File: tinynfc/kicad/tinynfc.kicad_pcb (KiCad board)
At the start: 2 copper layers, 28 x 28 mm, 15 parts, among them Q1 Diodes_DFN1006-3, U1 NXP_SOT902-3_XQFN8, U2 VQFN-20-1EP_3x3mm_P0.4mm_EP1.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

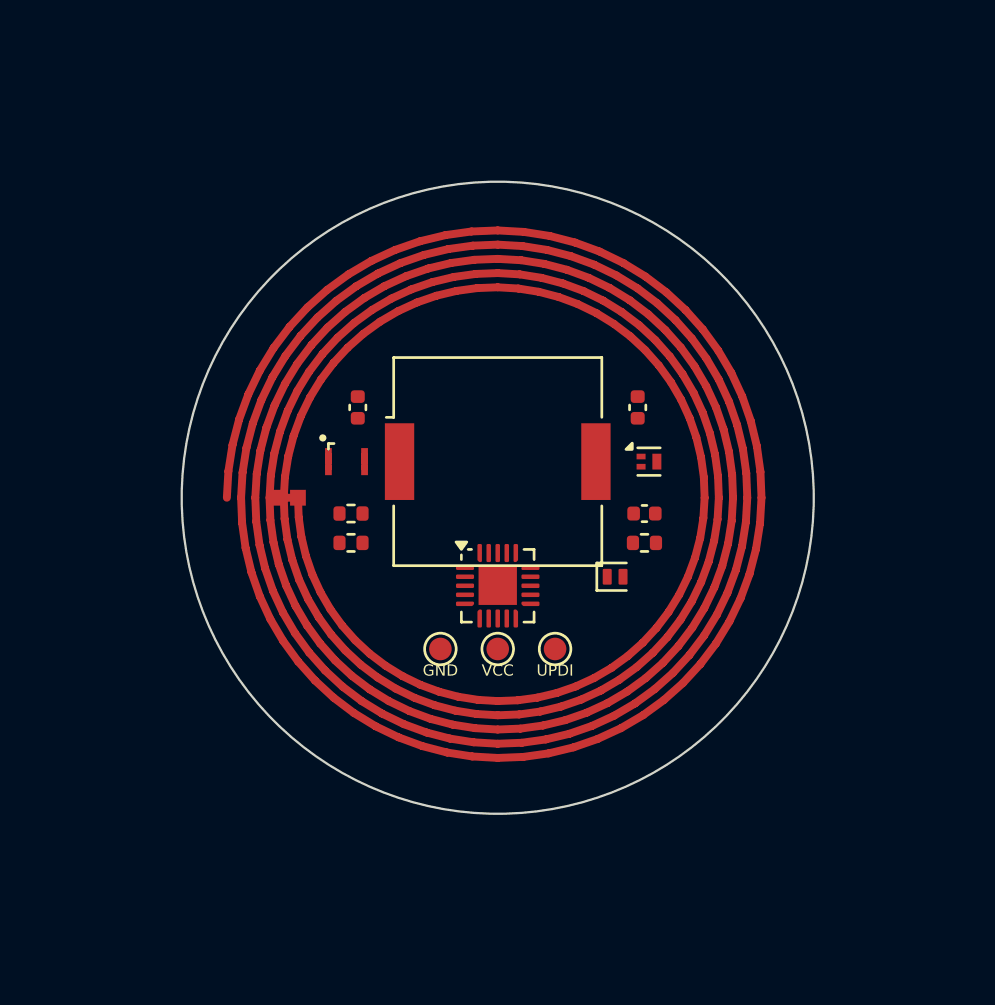
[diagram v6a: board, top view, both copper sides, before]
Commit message: Shrink TinyNFC board to exact US-quarter diameter
Trim the FR-4 ring outside the spiral: outline is Ø 24.26 mm, antenna
Ø 23 mm with ~0.5 mm copper-to-edge, parts pulled into the tighter island.

Co-authored-by: Jason Hall <imjasonh@users.noreply.github.com>
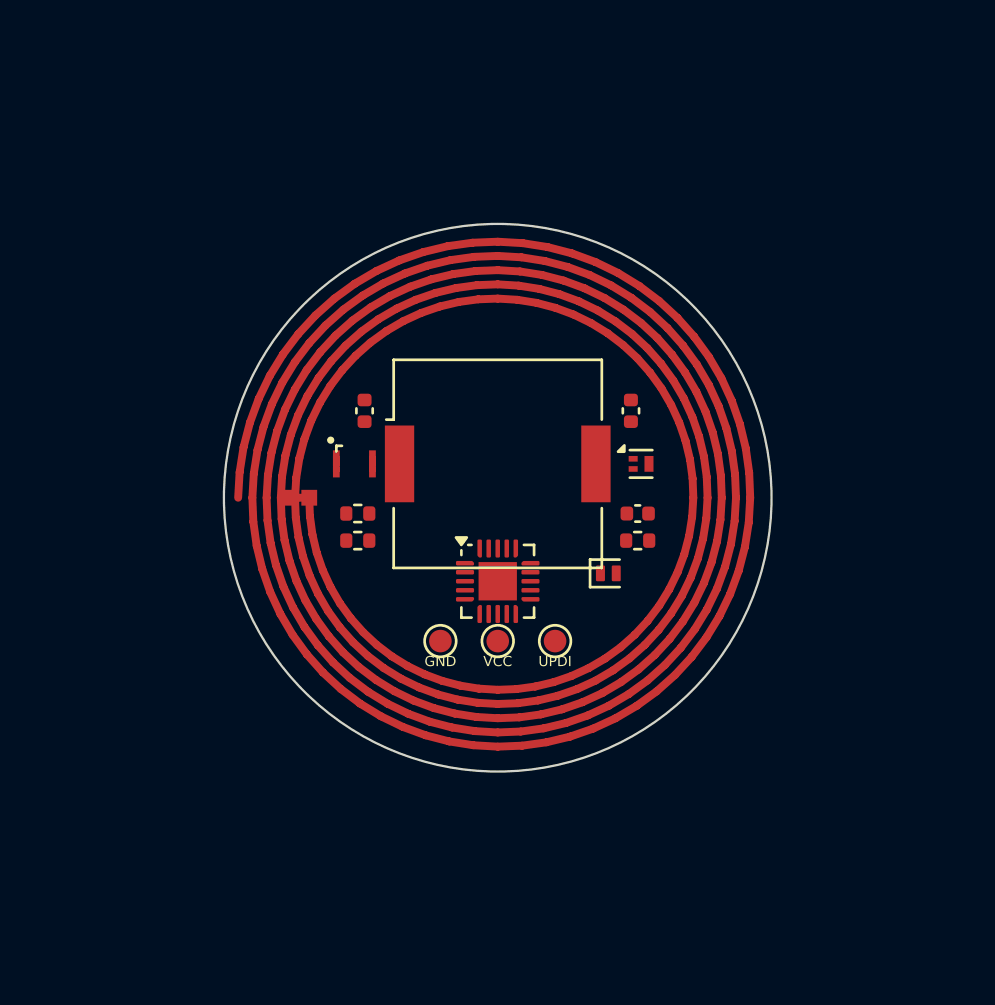
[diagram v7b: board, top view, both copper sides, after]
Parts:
- moved Q1 0.36 mm to (6.35, -1.50)
- moved U1 0.36 mm to (-6.35, -1.50)
- moved TP1 0.35 mm to (-2.54, 6.35)
- moved TP2 0.35 mm to (0.00, 6.35)
- moved TP3 0.35 mm to (2.54, 6.35)
- moved C1 0.34 mm to (-5.90, -3.85)
- moved C2 0.34 mm to (5.90, -3.85)
- moved D1 0.34 mm to (4.90, 3.35)
- moved R2 0.32 mm to (-6.20, 1.90)
- moved R3 0.32 mm to (6.20, 1.90)
- moved C3 0.30 mm to (6.20, 0.70)
- moved R1 0.30 mm to (-6.20, 0.70)
- moved U2 0.20 mm to (0.00, 3.70)
- moved PZ1 0.10 mm to (0.00, -1.50)
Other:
- board size 28 x 28 mm -> 24.3 x 24.3 mm
- board text added: "US quarter Ø24.26 mm"
- board text added: "board Ø24.26×1.6 mm"
- board text removed: "US quarter"
- board text removed: "board Ø28×1.6 mm"
- board text removed: "Ø24.26 mm"
